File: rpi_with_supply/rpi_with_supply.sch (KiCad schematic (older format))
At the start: 36 parts, among them J1 Phoenix 1934861, J2 Phoenix 1934861, J3 Phoenix 1933189 COMBICON, J4 Phoenix 1933189 COMBICON, J5 Raspberry_Pi_2_3, P1 CONN_1, P10 CONN_02X02, P2 CONN_1, P3 CONN_1, P4 CONN_1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

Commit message: update shcematic
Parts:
- added J6: FAN, Socket_Strip_Straight_1x02_Pitch2.54mm, symbol Conn_01x02
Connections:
- net GND: now also J6.1 (Pin_1)
- net PI_PWR: now also J6.2 (Pin_2)

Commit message: bump to rev b
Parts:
- removed U3: vn7040-switch, SOIC-8_3.9x4.9mm_Pitch1.27mm, symbol vn7040-switch
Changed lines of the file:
@@
 LIBS:switches
 LIBS:relays
-LIBS:motors
 LIBS:transistors
 LIBS:conn
@@
 LIBS:da4xbridge
 LIBS:11aa-unio-eeprom
+LIBS:ws2813
+LIBS:ts4231
+LIBS:xor_sot_353_74lvc1g86
 LIBS:ice40ul1k
 LIBS:esp32-wroom
@@
 LIBS:lm3478
 LIBS:tps40211
+LIBS:lm5110
+LIBS:vn7040-switch
 LIBS:rpi_with_supply-cache
 EELAYER 25 0
@@
 	1    0    0    -1
 $EndComp
-$Comp
-L vn7040-switch U3
-U 1 1 5B2D271D
-P 8150 4000
-F 0 "U3" H 7900 4250 60  0000 C CNN
-F 1 "vn7040-switch" H 8150 3750 60  0000 C CNN
-F 2 "SOIC-8_3.9x4.9mm_Pitch1.27mm" H 8150 4300 60  0000 C CNN
-F 3 "" H 8150 4000 60  0000 C CNN
-	1    8150 4000
-	1    0    0    -1
-$EndComp

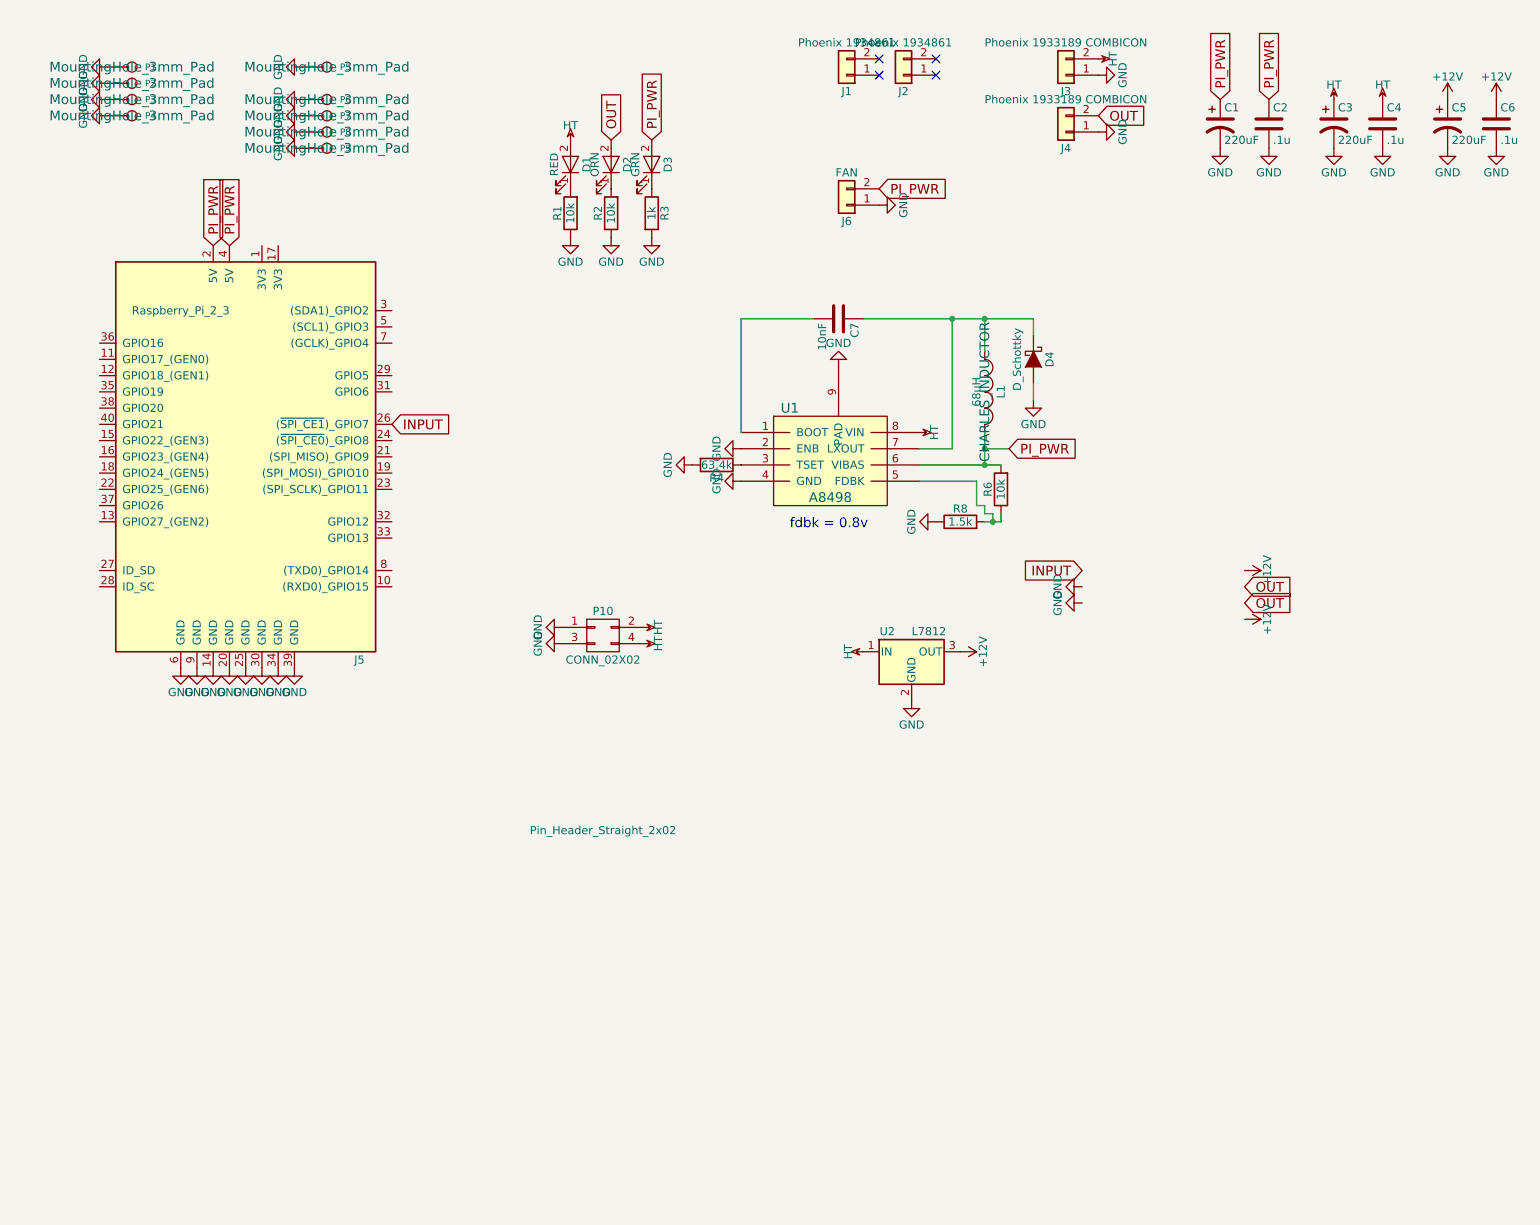
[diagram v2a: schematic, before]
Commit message: Bump design with pull up
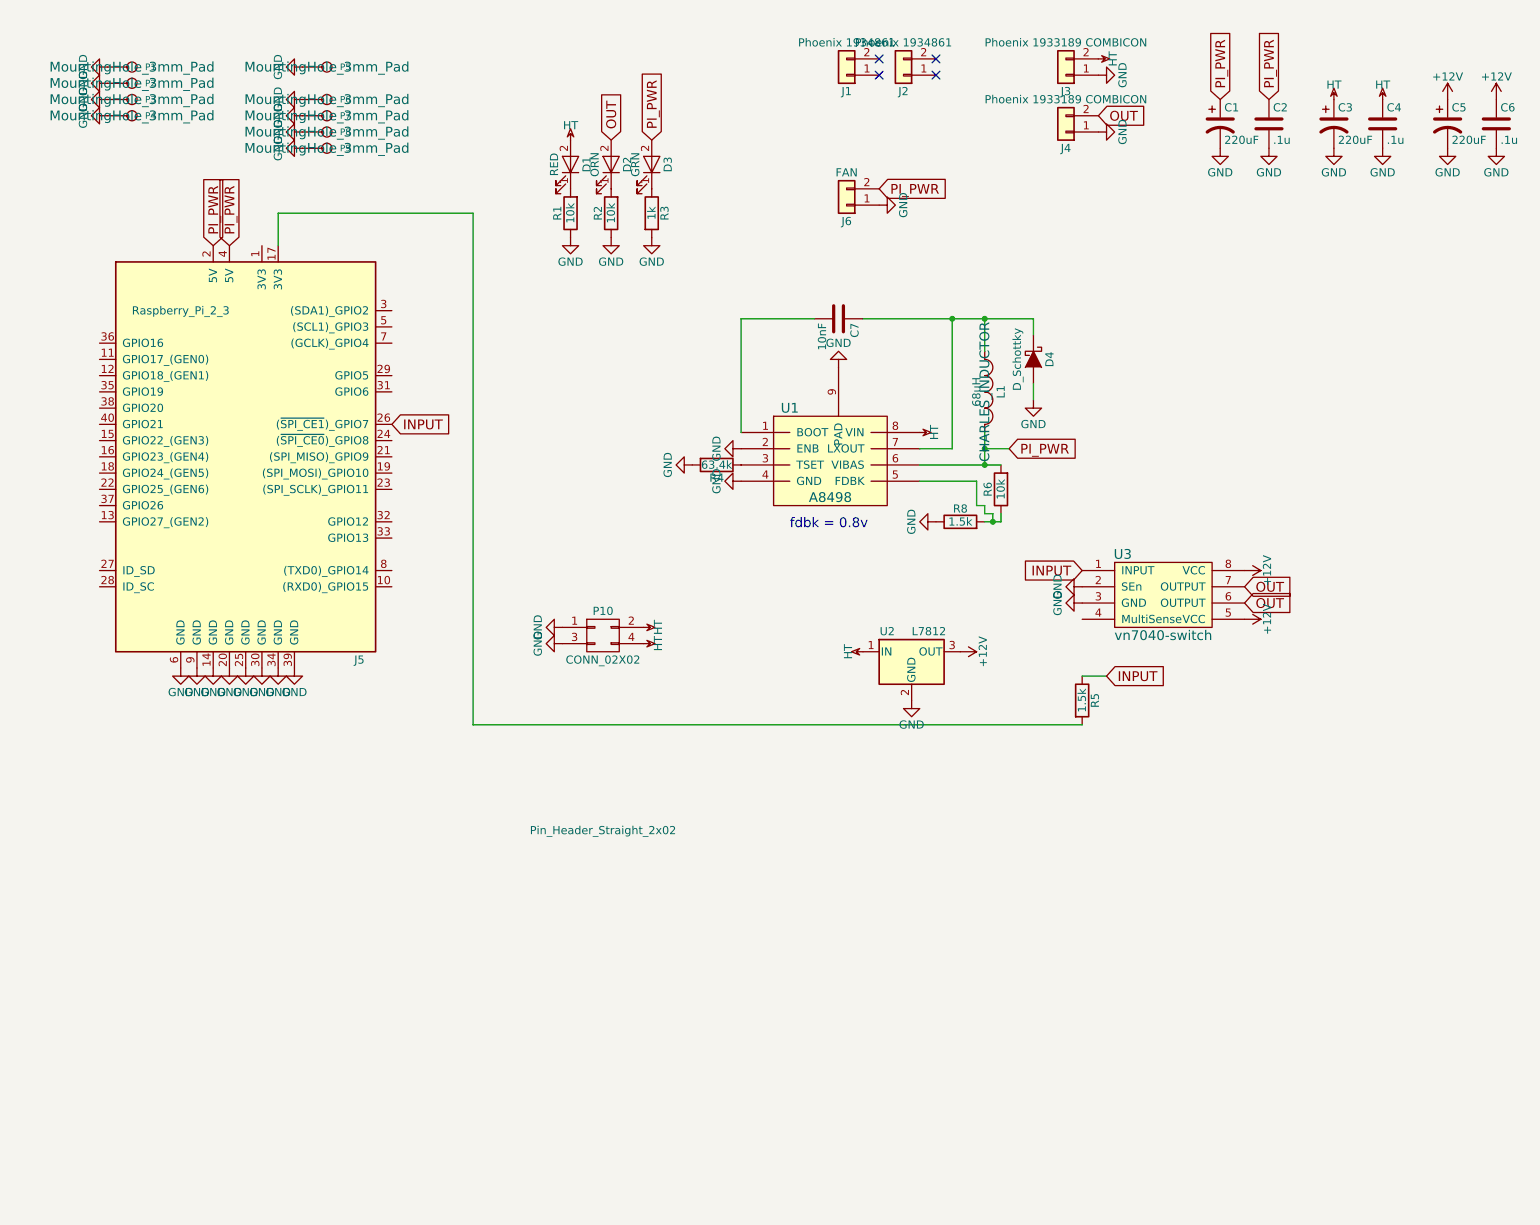
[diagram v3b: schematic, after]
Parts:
- added R5: 1.5k, R_0805, symbol R
- added U3: vn7040-switch, symbol vn7040-switch
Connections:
- net +12V: now also U3.5 (VCC), U3.8 (VCC)
- net GND: now also U3.2 (SEn), U3.3 (GND)
- net INPUT: now also R5.1, U3.1 (INPUT)
- net OUT: now also U3.6 (OUTPUT), U3.7 (OUTPUT)
- net at J5.17 (3V3): now also R5.2

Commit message: update design
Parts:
- added C8: .1u, C_0805, symbol C
- added D5: RED, LED_0805, symbol LED-RESCUE-rpi_with_supply
- added IC1: ATTINY85-S, SOIC-8-WIDE, symbol ATTINY85-S
- added P11: WS2812, Pin_Header_Straight_1x03, symbol CONN_01X03
- added Q1: Q_NMOS_GDS, SOT-23, symbol Q_NMOS_GDS
- added R7: 10k, R_0805, symbol R
- added R9: 1.5k, R_0805, symbol R
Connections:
- net GND: now also C8.2, IC1.4 (GND), P11.1 (P1), Q1.3 (S), R9.2; no longer J6.1 (Pin_1)
- net HT: now also R7.1
- net PI_PWR: now also D5.1 (K), P11.3 (P3)
- net +3V3: now reaches J5.17 (3V3), R5.2
- net +3V3: now also C8.1, IC1.8 (VCC)
- net MOSI: now reaches J5.19 ((SPI_MOSI)_GPIO10)
- net MOSI: now also IC1.5 (PB0(MOSI/DI/SDA/AIN0/OC0A/OC1A/AREF/PCINT0))
- net MISO: now reaches J5.21 ((SPI_MISO)_GPIO9)
- net MISO: now also IC1.6 (PB1(MISO/DO/AIN1/OC0B/OC1A/PCINT1))
- net SCK: now reaches J5.23 ((SPI_SCLK)_GPIO11)
- net SCK: now also IC1.7 (PB2(SCK/USCK/SCL/T0/INT0/ADC1/PCINT2))
- net ~AVRRST~: now reaches J5.24 ((~SPI_CE0~)_GPIO8)
- net ~AVRRST~: now also IC1.1 (PB5(~RESET~/dW/ADC0/PCINT5))
- new net: D5.2 (A), J6.1 (Pin_1), Q1.2 (D)
- new net: IC1.3 (PB4(XTAL2/CLKO/OC1B/ADC2/PCINT4)), P11.2 (P2), R7.2, R9.1
- new net FANCTL: IC1.2 (PB3(XTAL1/CLKI/OC1B/ADC3/PCINT3)), Q1.1 (G)
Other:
- moved on the sheet: J6
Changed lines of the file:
@@
 L Conn_01x02 J6
 U 1 1 5B690D14
-P 6200 1600
-F 0 "J6" H 6200 1700 50  0000 C CNN
-F 1 "FAN" H 6200 1400 50  0000 C CNN
-F 2 "Socket_Strip_Straight_1x02_Pitch2.54mm" H 6200 1600 50  0001 C CNN
-F 3 "" H 6200 1600 50  0001 C CNN
-	1    6200 1600
+P 4700 7200
+F 0 "J6" H 4700 7300 50  0000 C CNN
+F 1 "FAN" H 4700 7000 50  0000 C CNN
+F 2 "Socket_Strip_Straight_1x02_Pitch2.54mm" H 4700 7200 50  0001 C CNN
+F 3 "" H 4700 7200 50  0001 C CNN
+	1    4700 7200
 	-1   0    0    1
 $EndComp
@@
 L GND #PWR053
 U 1 1 5B690EB1
-P 6400 1600
-F 0 "#PWR053" H 6400 1350 50  0001 C CNN
-F 1 "GND" H 6400 1450 50  0000 C CNN
-F 2 "" H 6400 1600 50  0001 C CNN
-F 3 "" H 6400 1600 50  0001 C CNN
-	1    6400 1600
-	0    -1   -1   0
-$EndComp
-Text GLabel 6400 1500 2    60   Input ~ 0
-PI_PWR
+P 4900 7600
+F 0 "#PWR053" H 4900 7350 50  0001 C CNN
+F 1 "GND" H 4900 7450 50  0000 C CNN
+F 2 "" H 4900 7600 50  0001 C CNN
+F 3 "" H 4900 7600 50  0001 C CNN
+	1    4900 7600
+	1    0    0    -1
+$EndComp
 $Comp
 L vn7040-switch U3
@@
 Wire Wire Line
 	2700 1650 2700 1850
+$Comp
+L ATTINY85-S IC1
+U 1 1 5B83509F
+P 3900 6100
+F 0 "IC1" H 2750 6500 50  0000 C CNN
+F 1 "ATTINY85-S" H 4900 5700 50  0000 C CNN
+F 2 "SOIC-8-WIDE" H 4850 6100 50  0000 C CIN
+F 3 "" H 3900 6100 50  0000 C CNN
+	1    3900 6100
+	1    0    0    -1
+$EndComp
+$Comp
+L GND #PWR054
+U 1 1 5B8352B4
+P 5250 6350
+F 0 "#PWR054" H 5250 6100 50  0001 C CNN
+F 1 "GND" H 5250 6200 50  0000 C CNN
+F 2 "" H 5250 6350 50  0001 C CNN
+F 3 "" H 5250 6350 50  0001 C CNN
+	1    5250 6350
+	1    0    0    -1
+$EndComp
+$Comp
+L +3.3V #PWR055
+U 1 1 5B835CCF
+P 4300 4700
+F 0 "#PWR055" H 4300 4550 50  0001 C CNN
+F 1 "+3.3V" H 4300 4840 50  0000 C CNN
+F 2 "" H 4300 4700 50  0000 C CNN
+F 3 "" H 4300 4700 50  0000 C CNN
+	1    4300 4700
+	1    0    0    -1
+$EndComp
+$Comp
+L +3.3V #PWR056
+U 1 1 5B835D56
+P 5250 5850
+F 0 "#PWR056" H 5250 5700 50  0001 C CNN
+F 1 "+3.3V" H 5250 5990 50  0000 C CNN
+F 2 "" H 5250 5850 50  0000 C CNN
+F 3 "" H 5250 5850 50  0000 C CNN
+	1    5250 5850
+	1    0    0    -1
+$EndComp
+Text GLabel 3400 3150 2    60   Input ~ 0
+MISO
+Text GLabel 3400 3250 2    60   Input ~ 0
+MOSI
+Text GLabel 3400 3350 2    60   Input ~ 0
+SCK
+Text GLabel 2550 5950 0    60   Input ~ 0
+MISO
+Text GLabel 2550 5850 0    60   Input ~ 0
+MOSI
+Text GLabel 2550 6050 0    60   Input ~ 0
+SCK
+$Comp
+L C C8
+U 1 1 5B83826A
+P 5600 6150
+F 0 "C8" H 5625 6250 50  0000 L CNN
+F 1 ".1u" H 5625 6050 50  0000 L CNN
+F 2 "C_0805" H 5638 6000 50  0001 C CNN
+F 3 "" H 5600 6150 50  0001 C CNN
+	1    5600 6150
+	1    0    0    -1
+$EndComp
+$Comp
+L +3.3V #PWR057
+U 1 1 5B838422
+P 5600 6000
+F 0 "#PWR057" H 5600 5850 50  0001 C CNN
+F 1 "+3.3V" H 5600 6140 50  0000 C CNN
+F 2 "" H 5600 6000 50  0000 C CNN
+F 3 "" H 5600 6000 50  0000 C CNN
+	1    5600 6000
+	1    0    0    -1
+$EndComp
+$Comp
+L GND #PWR058
+U 1 1 5B8384A5
+P 5600 6300
+F 0 "#PWR058" H 5600 6050 50  0001 C CNN
+F 1 "GND" H 5600 6150 50  0000 C CNN
+F 2 "" H 5600 6300 50  0001 C CNN
+F 3 "" H 5600 6300 50  0001 C CNN
+	1    5600 6300
+	1    0    0    -1
+$EndComp
+Text GLabel 3400 3050 2    60   Input ~ 0
+~AVRRST~
+Text GLabel 2550 6350 0    60   Input ~ 0
+~AVRRST~
+Text GLabel 4900 7100 2    60   Input ~ 0
+PI_PWR
+$Comp
+L Q_NMOS_GDS Q1
+U 1 1 5B83A81E
+P 4800 7400
+F 0 "Q1" H 5100 7450 50  0000 R CNN
+F 1 "Q_NMOS_GDS" H 5450 7350 50  0000 R CNN
+F 2 "SOT-23" H 5000 7500 50  0000 C CNN
+F 3 "" H 4800 7400 50  0000 C CNN
+	1    4800 7400
+	1    0    0    -1
+$EndComp
+Text GLabel 4600 7400 0    60   Input ~ 0
+FANCTL
+Text GLabel 2550 6150 0    60   Input ~ 0
+FANCTL
+Wire Wire Line
+	2550 6250 1950 6250
+$Comp
+L R R7
+U 1 1 5B83EBD4
+P 1950 6100
+F 0 "R7" V 2030 6100 50  0000 C CNN
+F 1 "10k" V 1950 6100 50  0000 C CNN
+F 2 "R_0805" V 1880 6100 50  0001 C CNN
+F 3 "" H 1950 6100 50  0001 C CNN
+	1    1950 6100
+	1    0    0    -1
+$EndComp
+$Comp
+L R R9
+U 1 1 5B83EC98
+P 2000 6450
+F 0 "R9" V 2080 6450 50  0000 C CNN
+F 1 "1.5k" V 2000 6450 50  0000 C CNN
+F 2 "R_0805" V 1930 6450 50  0001 C CNN
+F 3 "" H 2000 6450 50  0001 C CNN
+	1    2000 6450
+	1    0    0    -1
+$EndComp
+Wire Wire Line
+	2000 6300 2000 6250
+Connection ~ 2000 6250
+$Comp
+L GND #PWR059
+U 1 1 5B840229
+P 2000 6600
+F 0 "#PWR059" H 2000 6350 50  0001 C CNN
+F 1 "GND" H 2000 6450 50  0000 C CNN
+F 2 "" H 2000 6600 50  0001 C CNN
+F 3 "" H 2000 6600 50  0001 C CNN
+	1    2000 6600
+	1    0    0    -1
+$EndComp
+$Comp
+L HT #PWR060
+U 1 1 5B8402E0
+P 1950 5950
+F 0 "#PWR060" H 1950 6070 50  0001 C CNN
+F 1 "HT" H 1950 6040 50  0000 C CNN
+F 2 "" H 1950 5950 50  0001 C CNN
+F 3 "" H 1950 5950 50  0001 C CNN
+	1    1950 5950
+	1    0    0    -1
+$EndComp
+$Comp
+L CONN_01X03 P11
+U 1 1 5B842054
+P 2700 7250
+F 0 "P11" H 2700 7450 50  0000 C CNN
+F 1 "WS2812" V 2800 7250 50  0000 C CNN
+F 2 "Pin_Header_Straight_1x03" H 2700 7250 50  0000 C CNN
+F 3 "" H 2700 7250 50  0000 C CNN
+	1    2700 7250
+	-1   0    0    1
+$EndComp
+$Comp
+L GND #PWR061
+U 1 1 5B8421B7
+P 2900 7350
+F 0 "#PWR061" H 2900 7100 50  0001 C CNN
+F 1 "GND" H 2900 7200 50  0000 C CNN
+F 2 "" H 2900 7350 50  0001 C CNN
+F 3 "" H 2900 7350 50  0001 C CNN
+	1    2900 7350
+	1    0    0    -1
+$EndComp
+Text GLabel 2900 7150 1    60   Input ~ 0
+PI_PWR
+Wire Wire Line
+	2100 6250 2100 6700
+Wire Wire Line
+	2100 6700 3500 6700
+Wire Wire Line
+	3500 6700 3500 7250
+Wire Wire Line
+	3500 7250 2900 7250
+Connection ~ 2100 6250
+Wire Wire Line
+	4300 4700 4300 4800
+Connection ~ 4300 4800
+$Comp
+L LED-RESCUE-rpi_with_supply D5
+U 1 1 5B849114
+P 5750 7150
+F 0 "D5" H 5750 7250 50  0000 C CNN
+F 1 "RED" H 5750 7050 50  0000 C CNN
+F 2 "LED_0805" H 5750 7150 50  0001 C CNN
+F 3 "" H 5750 7150 50  0001 C CNN
+	1    5750 7150
+	0    1    -1   0
+$EndComp
+Text GLabel 5750 7300 2    60   Input ~ 0
+PI_PWR
+Wire Wire Line
+	4900 7200 5400 7200
+Wire Wire Line
+	5400 7200 5400 7000
+Wire Wire Line
+	5400 7000 5750 7000
 $EndSCHEMATC

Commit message: bump
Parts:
- IC1: value ATTINY85-S -> ATTINY25
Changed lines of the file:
@@
 P 3900 6100
 F 0 "IC1" H 2750 6500 50  0000 C CNN
-F 1 "ATTINY85-S" H 4900 5700 50  0000 C CNN
+F 1 "ATTINY25" H 4900 5700 50  0000 C CNN
 F 2 "SOIC-8-WIDE" H 4850 6100 50  0000 C CIN
 F 3 "" H 3900 6100 50  0000 C CNN

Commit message: bump
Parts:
- removed Q1: Q_NMOS_GDS, SOT-23, symbol Q_NMOS_GDS
- added Q1: 2N7002, SOT-23, symbol Q_NMOS_GSD
- added SW1: PWR, TACTILE10, symbol TACTILE
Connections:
- net FANCTL: now also Q1.1 (G)
- net GND: now also Q1.2 (S), SW1.1
- net 3V3: now reaches J5.1 (3V3)
- net GPIO15: now reaches J5.10 ((RXD0)_GPIO15)
- net GPIO17: now reaches J5.11 (GPIO17_(GEN0))
- net GPIO18: now reaches J5.12 (GPIO18_(GEN1))
- net GPIO27: now reaches J5.13 (GPIO27_(GEN2))
- net GPIO22: now reaches J5.15 (GPIO22_(GEN3))
- net GPIO23: now reaches J5.16 (GPIO23_(GEN4))
- net GPIO24: now reaches J5.18 (GPIO24_(GEN5))
- net GPIO25: now reaches J5.22 (GPIO25_(GEN6))
- net GPIO5: now reaches J5.29 (GPIO5)
- net GPIO2: now reaches J5.3 ((SDA1)_GPIO2)
- net GPIO6: now reaches J5.31 (GPIO6)
- net GPIO12: now reaches J5.32 (GPIO12)
- net GPIO13: now reaches J5.33 (GPIO13)
- net GPIO19: now reaches J5.35 (GPIO19)
- net GPIO16: now reaches J5.36 (GPIO16)
- net GPIO26: now reaches J5.37 (GPIO26)
- net GPIO20: now reaches J5.38 (GPIO20)
- net GPIO21: now reaches J5.40 (GPIO21)
- net GPIO21: now also SW1.4
- net GPIO3: now reaches J5.5 ((SCL1)_GPIO3)
- net GPIO4: now reaches J5.7 ((GCLK)_GPIO4)
- net GPIO14: now reaches J5.8 ((TXD0)_GPIO14)
- net at D5.2 (A), J6.1 (Pin_1): now also Q1.3 (D)
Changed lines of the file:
@@
 	7800 4500 7650 4500
 Wire Wire Line
-	7650 4800 3900 4800
+	3900 4800 7650 4800
 Wire Wire Line
 	3900 4800 3900 1650
@@
 Text GLabel 4900 7100 2    60   Input ~ 0
 PI_PWR
-$Comp
-L Q_NMOS_GDS Q1
-U 1 1 5B83A81E
-P 4800 7400
-F 0 "Q1" H 5100 7450 50  0000 R CNN
-F 1 "Q_NMOS_GDS" H 5450 7350 50  0000 R CNN
-F 2 "SOT-23" H 5000 7500 50  0000 C CNN
-F 3 "" H 4800 7400 50  0000 C CNN
-	1    4800 7400
-	1    0    0    -1
-$EndComp
 Text GLabel 4600 7400 0    60   Input ~ 0
 FANCTL
@@
 FANCTL
 Wire Wire Line
-	2550 6250 1950 6250
+	1950 6250 2550 6250
 $Comp
 L R R7
@@
 Wire Wire Line
 	5400 7000 5750 7000
+$Comp
+L Q_NMOS_GSD Q1
+U 1 1 5BB46437
+P 4800 7400
+F 0 "Q1" H 5100 7450 50  0000 R CNN
+F 1 "2N7002" H 5450 7350 50  0000 R CNN
+F 2 "SOT-23" H 5000 7500 50  0000 C CNN
+F 3 "" H 4800 7400 50  0000 C CNN
+	1    4800 7400
+	1    0    0    -1
+$EndComp
+Text GLabel 3400 2650 2    60   Input ~ 0
+GPIO5
+Text GLabel 3400 2450 2    60   Input ~ 0
+GPIO4
+Text GLabel 3400 2350 2    60   Input ~ 0
+GPIO3
+Text GLabel 3400 2250 2    60   Input ~ 0
+GPIO2
+Text GLabel 3400 2750 2    60   Input ~ 0
+GPIO6
+Text GLabel 3400 3550 2    60   Input ~ 0
+GPIO12
+Text GLabel 3400 3650 2    60   Input ~ 0
+GPIO13
+Text GLabel 3400 3850 2    60   Input ~ 0
+GPIO14
+Text GLabel 3400 3950 2    60   Input ~ 0
+GPIO15
+Text GLabel 1600 3550 0    60   Input ~ 0
+GPIO27
+Text GLabel 1600 3450 0    60   Input ~ 0
+GPIO26
+Text GLabel 1600 3350 0    60   Input ~ 0
+GPIO25
+Text GLabel 1600 3250 0    60   Input ~ 0
+GPIO24
+Text GLabel 1600 3150 0    60   Input ~ 0
+GPIO23
+Text GLabel 1600 3050 0    60   Input ~ 0
+GPIO22
+Text GLabel 1600 2950 0    60   Input ~ 0
+GPIO21
+Text GLabel 1600 2850 0    60   Input ~ 0
+GPIO20
+Text GLabel 1600 2750 0    60   Input ~ 0
+GPIO19
+Text GLabel 1600 2650 0    60   Input ~ 0
+GPIO18
+Text GLabel 1600 2550 0    60   Input ~ 0
+GPIO17
+Text GLabel 1600 2450 0    60   Input ~ 0
+GPIO16
+Text GLabel 2600 1850 1    60   Input ~ 0
+3V3
+$Comp
+L TACTILE SW1
+U 1 1 5BC5CC6A
+P 9200 5650
+F 0 "SW1" H 9200 5500 60  0000 C CNN
+F 1 "PWR" H 9200 5800 60  0000 C CNN
+F 2 "TACTILE10" H 9200 5650 60  0000 C CNN
+F 3 "" H 9200 5650 60  0000 C CNN
+	1    9200 5650
+	1    0    0    -1
+$EndComp
+$Comp
+L GND #PWR062
+U 1 1 5BC5D089
+P 8900 5550
+F 0 "#PWR062" H 8900 5300 50  0001 C CNN
+F 1 "GND" H 8900 5400 50  0000 C CNN
+F 2 "" H 8900 5550 50  0001 C CNN
+F 3 "" H 8900 5550 50  0001 C CNN
+	1    8900 5550
+	0    1    1    0
+$EndComp
+Text GLabel 9500 5750 2    60   Input ~ 0
+GPIO21
 $EndSCHEMATC

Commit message: bump design
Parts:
- removed D3: GRN, LED_0805, symbol LED-RESCUE-rpi_with_supply
- removed R5: 1.5k, R_0805, symbol R
- added D6: BLU, LED_0805, symbol LED-RESCUE-rpi_with_supply
- added P12: UPDI, Pin_Header_Straight_1x03, symbol CONN_01X03
- added Q2: FDV304P, SOT-23, symbol Q_PMOS_GSD
- added Q3: DMN2046, SOT-23, symbol Q_NMOS_GSD
- added R10: 1k, R_0805, symbol R
- added R11: 10k, R_0805, symbol R
- Q1: value 2N7002 -> DMN2046; Digikey (none) -> DMN2046U-7DICT-ND
- R3: value 1k -> 10k
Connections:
- net +3V3: now also P12.1 (P1)
- net GND: now also D6.1 (K), P12.3 (P3), Q3.2 (S); no longer R3.2
- net GPIO17: now also Q3.1 (G)
- net HT: now also R3.2, Q2.3 (D)
- net at R3.1: now also Q2.1 (G), Q3.3 (D)
- net 3V3: no longer names the net of J5.1 (3V3)
- net GPIO14: no longer names the net of J5.8 ((TXD0)_GPIO14)
- net GPIO14: now also R11.1
- net GPIO15 renamed TXRX
- net TXRX: now also R10.1, R11.2
- new net: P12.2 (P2), Q2.2 (S), R10.2
